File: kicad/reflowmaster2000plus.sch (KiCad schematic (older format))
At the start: 21 parts, among them IC1 TLP3063, P1 CONN_8, P2 Toaster, P3 220V, U1 TRIAC, U2 TLC2272

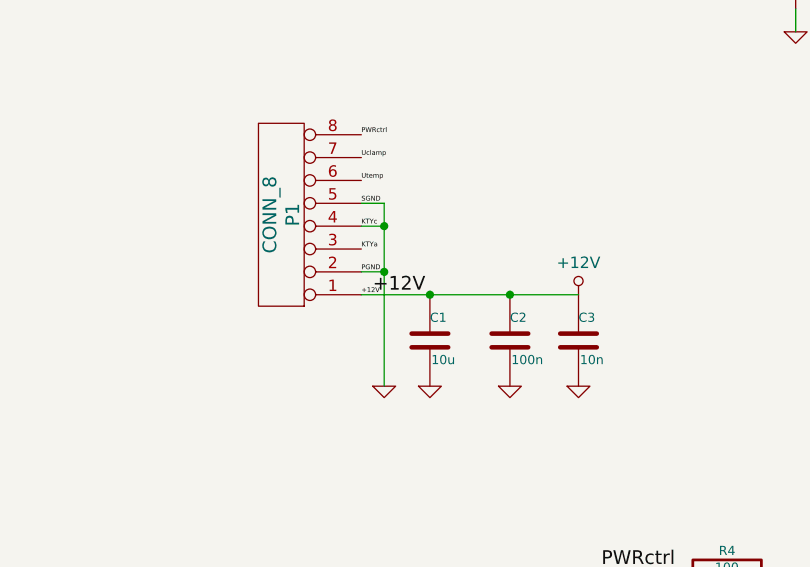
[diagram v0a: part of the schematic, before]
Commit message: [enh] compressed pcb into 5x2.5cm
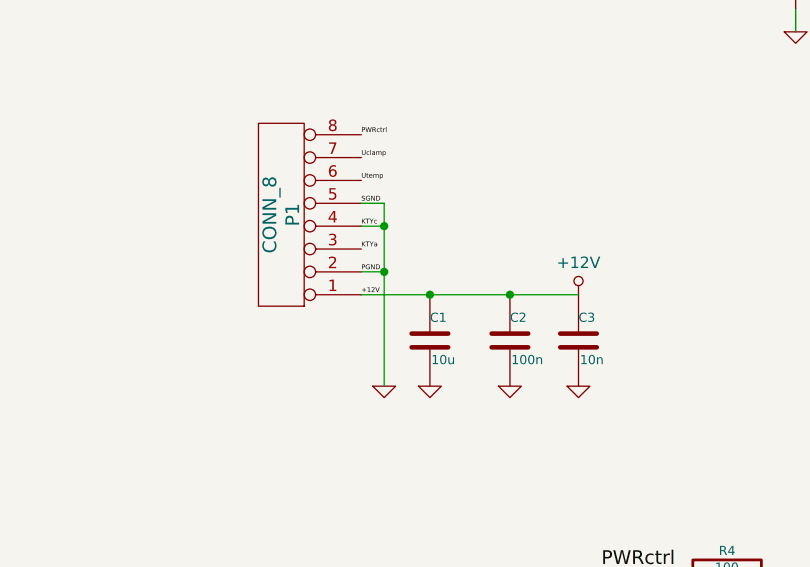
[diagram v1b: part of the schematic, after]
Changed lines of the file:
@@
 LIBS:memory
 LIBS:xilinx
+LIBS:special
 LIBS:microcontrollers
 LIBS:dsp
@@
 LIBS:hc11
 LIBS:logo
+LIBS:microchip1
 LIBS:microchip_pic10mcu
 LIBS:microchip_pic12mcu
@@
 LIBS:ttl_ieee
 LIBS:video
+LIBS:my
 LIBS:reflowmaster2000plus-cache
-EELAYER 25 0
+EELAYER 27 0
 EELAYER END
 $Descr A4 11693 8268
@@
 	1    0    0    -1
 $EndComp
-Text Label 3350 4800 0    60   ~ 0
-+12V
 Text Label 3300 4800 0    21   ~ 0
 +12V

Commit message: [enh] lot's of polishing
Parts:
- R4: value 100 -> 330
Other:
- moved on the sheet: C1, C2, C3
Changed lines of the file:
@@
 LIBS:ttl_ieee
 LIBS:video
+LIBS:reflowmaster2000plus-cache
 LIBS:my
 LIBS:reflowmaster2000plus-cache
@@
 F 3 "~" H 5500 6000 60  0000 C CNN
 	1    5500 6000
-	-1   0    0    1
+	1    0    0    1
 $EndComp
 $Comp
@@
 P 4900 6000
 F 0 "R4" V 4980 6000 40  0000 C CNN
-F 1 "100" V 4907 6001 40  0000 C CNN
+F 1 "330" V 4907 6001 40  0000 C CNN
 F 2 "~" V 4830 6000 30  0000 C CNN
 F 3 "~" H 4900 6000 30  0000 C CNN
@@
 L C-RESCUE-reflowmaster2000plus C1
 U 1 1 55610525
-P 3600 5000
-F 0 "C1" H 3600 5100 40  0000 L CNN
-F 1 "10u" H 3606 4915 40  0000 L CNN
-F 2 "~" H 3638 4850 30  0000 C CNN
-F 3 "~" H 3600 5000 60  0000 C CNN
-	1    3600 5000
+P 3600 4400
+F 0 "C1" H 3600 4500 40  0000 L CNN
+F 1 "10u" H 3606 4315 40  0000 L CNN
+F 2 "~" H 3638 4250 30  0000 C CNN
+F 3 "~" H 3600 4400 60  0000 C CNN
+	1    3600 4400
 	1    0    0    -1
 $EndComp
@@
 L C-RESCUE-reflowmaster2000plus C2
 U 1 1 55610534
-P 3950 5000
-F 0 "C2" H 3950 5100 40  0000 L CNN
-F 1 "100n" H 3956 4915 40  0000 L CNN
-F 2 "~" H 3988 4850 30  0000 C CNN
-F 3 "~" H 3950 5000 60  0000 C CNN
-	1    3950 5000
+P 3950 4400
+F 0 "C2" H 3950 4500 40  0000 L CNN
+F 1 "100n" H 3956 4315 40  0000 L CNN
+F 2 "~" H 3988 4250 30  0000 C CNN
+F 3 "~" H 3950 4400 60  0000 C CNN
+	1    3950 4400
 	1    0    0    -1
 $EndComp
@@
 L C-RESCUE-reflowmaster2000plus C3
 U 1 1 55610543
-P 4250 5000
-F 0 "C3" H 4250 5100 40  0000 L CNN
-F 1 "10n" H 4256 4915 40  0000 L CNN
-F 2 "~" H 4288 4850 30  0000 C CNN
-F 3 "~" H 4250 5000 60  0000 C CNN
-	1    4250 5000
+P 4250 4400
+F 0 "C3" H 4250 4500 40  0000 L CNN
+F 1 "10n" H 4256 4315 40  0000 L CNN
+F 2 "~" H 4288 4250 30  0000 C CNN
+F 3 "~" H 4250 4400 60  0000 C CNN
+	1    4250 4400
 	1    0    0    -1
 $EndComp
@@
 L GND-RESCUE-reflowmaster2000plus #PWR03
 U 1 1 55610585
-P 3600 5200
-F 0 "#PWR03" H 3600 5200 30  0001 C CNN
-F 1 "GND" H 3600 5130 30  0001 C CNN
-F 2 "" H 3600 5200 60  0000 C CNN
-F 3 "" H 3600 5200 60  0000 C CNN
-	1    3600 5200
+P 3600 4600
+F 0 "#PWR03" H 3600 4600 30  0001 C CNN
+F 1 "GND" H 3600 4530 30  0001 C CNN
+F 2 "" H 3600 4600 60  0000 C CNN
+F 3 "" H 3600 4600 60  0000 C CNN
+	1    3600 4600
 	1    0    0    -1
 $EndComp
@@
 L GND-RESCUE-reflowmaster2000plus #PWR04
 U 1 1 55610594
-P 3950 5200
-F 0 "#PWR04" H 3950 5200 30  0001 C CNN
-F 1 "GND" H 3950 5130 30  0001 C CNN
-F 2 "" H 3950 5200 60  0000 C CNN
-F 3 "" H 3950 5200 60  0000 C CNN
-	1    3950 5200
+P 3950 4600
+F 0 "#PWR04" H 3950 4600 30  0001 C CNN
+F 1 "GND" H 3950 4530 30  0001 C CNN
+F 2 "" H 3950 4600 60  0000 C CNN
+F 3 "" H 3950 4600 60  0000 C CNN
+	1    3950 4600
 	1    0    0    -1
 $EndComp
@@
 L GND-RESCUE-reflowmaster2000plus #PWR05
 U 1 1 556105A3
-P 4250 5200
-F 0 "#PWR05" H 4250 5200 30  0001 C CNN
-F 1 "GND" H 4250 5130 30  0001 C CNN
-F 2 "" H 4250 5200 60  0000 C CNN
-F 3 "" H 4250 5200 60  0000 C CNN
-	1    4250 5200
-	1    0    0    -1
-$EndComp
-Text Label 3300 4800 0    21   ~ 0
+P 4250 4600
+F 0 "#PWR05" H 4250 4600 30  0001 C CNN
+F 1 "GND" H 4250 4530 30  0001 C CNN
+F 2 "" H 4250 4600 60  0000 C CNN
+F 3 "" H 4250 4600 60  0000 C CNN
+	1    4250 4600
+	1    0    0    -1
+$EndComp
+Text Label 3400 4200 0    21   ~ 0
 +12V
 Text Label 3300 4700 0    21   ~ 0
 PGND
-Text Label 3300 4600 0    21   ~ 0
+Text Label 3300 4800 0    21   ~ 0
 KTYa
 Text Label 3300 4500 0    21   ~ 0
 KTYc
 Text Label 3300 4400 0    21   ~ 0
-SGND
+Utemp
 Text Label 3300 4300 0    21   ~ 0
-Utemp
-Text Label 3300 4200 0    21   ~ 0
 Uclamp
 $Comp
@@
 L +12V #PWR09
 U 1 1 556342B0
-P 4250 4800
-F 0 "#PWR09" H 4250 4650 50  0001 C CNN
-F 1 "+12V" H 4250 4940 50  0000 C CNN
-F 2 "" H 4250 4800 60  0000 C CNN
-F 3 "" H 4250 4800 60  0000 C CNN
-	1    4250 4800
+P 4250 4200
+F 0 "#PWR09" H 4250 4050 50  0001 C CNN
+F 1 "+12V" H 4250 4340 50  0000 C CNN
+F 2 "" H 4250 4200 60  0000 C CNN
+F 3 "" H 4250 4200 60  0000 C CNN
+	1    4250 4200
 	1    0    0    -1
 $EndComp
@@
 	5400 2100 6700 2100
 Wire Wire Line
-	3300 4800 4250 4800
-Connection ~ 3600 4800
-Connection ~ 3950 4800
-Wire Wire Line
-	3300 4400 3400 4400
+	3300 4200 4250 4200
+Connection ~ 3600 4200
+Connection ~ 3950 4200
 Wire Wire Line
 	3400 4700 3300 4700
@@
 	8450 5600 8100 5600
 Wire Wire Line
-	3400 4400 3400 5200
+	3400 4500 3400 5200
 Wire Wire Line
 	9100 3650 9100 3550
@@
 Wire Wire Line
 	3300 4500 3400 4500
-Connection ~ 3400 4500
 Wire Wire Line
 	9100 4200 9100 3950
@@
 	1    0    0    -1
 $EndComp
+Wire Wire Line
+	3300 4600 3400 4600
+Connection ~ 3400 4600
+Text Label 3300 4600 0    21   ~ 0
+SGND
 $EndSCHEMATC

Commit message: [enh] merged schema blocks into one
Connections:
- wire segments 43 -> 45
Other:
- moved on the sheet: C1, C2, C3, D1, D2, D3, IC1, P1, P2, P3, R1, R2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

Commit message: SCH and PCB almost completely redrawn. Moved symbols and components to a separate lib.
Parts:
- removed D2: BAT46, ~, symbol ZENER
- removed D3: BZX55C5V1, ~, symbol SCHOTTKY
- removed D4: VREFDIODE, ~, symbol VREFDIODE
- removed IC1: TLP3063, DIP6, symbol MOC3033M-RESCUE-reflowmaster2000plus
- removed P1: CONN_8, symbol CONN_8
- removed P2: Toaster, symbol CONN_2
- removed P3: 220V, symbol CONN_2
- removed R7: 330, ~, symbol R-RESCUE-reflowmaster2000plus
- removed RV1, RV3: 500, ~, symbol POT
- removed U1: TRIAC, ~, symbol TRIAC
- added D1: LM385-1.2, rf2kpdp:TO-92_LE33CZ, symbol LM385-1.2
- added D2: BAT46, rf2kpdp:SOD-80, symbol BAT46
- added D3: C5V6, rf2kpdp:SOD-80, symbol C5V6
- added P1: CONN_02X04, rf2kpdp:Pin_Header_Straight_2x04, symbol CONN_02X04
- added P2: 230V, rf2kpdp:1pin-small, symbol CONN_1
- added P3: Toaster, rf2kpdp:1pin-small, symbol CONN_1
- added R2: 500, rf2kpdp:SM0805-R, symbol R
- added U2: MOC3063M, rf2kpdp:DIP-6__300, symbol MOC3063M
- added U3: BTA24, rf2kpdp:TO220AB_BTA24, symbol BTA24-600
- C1, C2, C3: footprint ~ -> rf2kpdp:SM0805-C; symbol C-RESCUE-reflowmaster2000plus -> C
- D4: renamed from D1; footprint ~ -> rf2kpdp:LED-3MM
- R1: renamed from R6; footprint ~ -> rf2kpdp:SM0805-R; symbol R-RESCUE-reflowmaster2000plus -> R
- R3: renamed from R2; value 330 -> 500; footprint ~ -> rf2kpdp:SM0805-R; symbol R-RESCUE-reflowmaster2000plus -> R
- R4: renamed from R5; value 4.7k -> 1k; footprint ~ -> rf2kpdp:SM0805-R; symbol R-RESCUE-reflowmaster2000plus -> R
- R5: renamed from R4; value 330 -> 500; footprint ~ -> rf2kpdp:SM0805-R; symbol R-RESCUE-reflowmaster2000plus -> R
- R6: renamed from R1; footprint ~ -> rf2kpdp:Resistor_Horizontal_RM10mm; symbol R-RESCUE-reflowmaster2000plus -> R
- U1: renamed from U2; footprint (none) -> rf2kpdp:SO8E
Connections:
- net labels removed: GNDPWR
- wire segments 45 -> 43
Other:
- note added: "<-2.4 mA"
- moved on the sheet: D4, U1A, U1B
